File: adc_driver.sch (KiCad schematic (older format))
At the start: 30 parts, among them U17 DG412xUE, U18 AD8421ARZ, U22 TMUX6136PWR, U24 LMP8350MA_NOPB

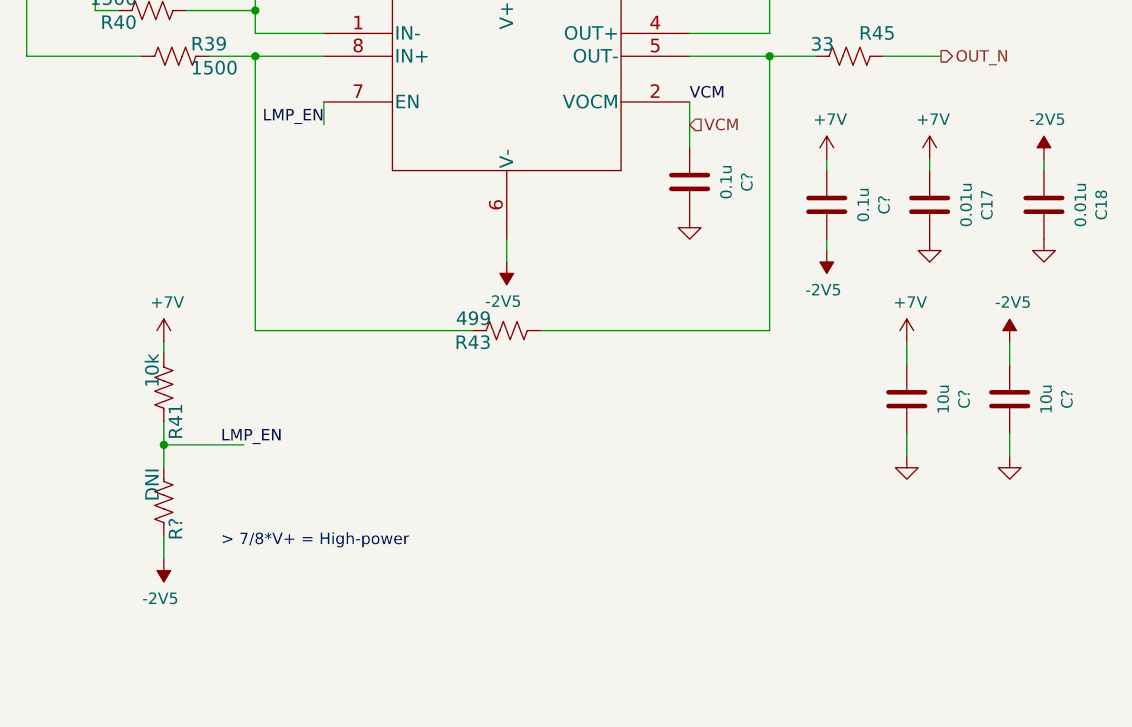
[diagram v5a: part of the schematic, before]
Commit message: clamp files at submission to JLCPCB
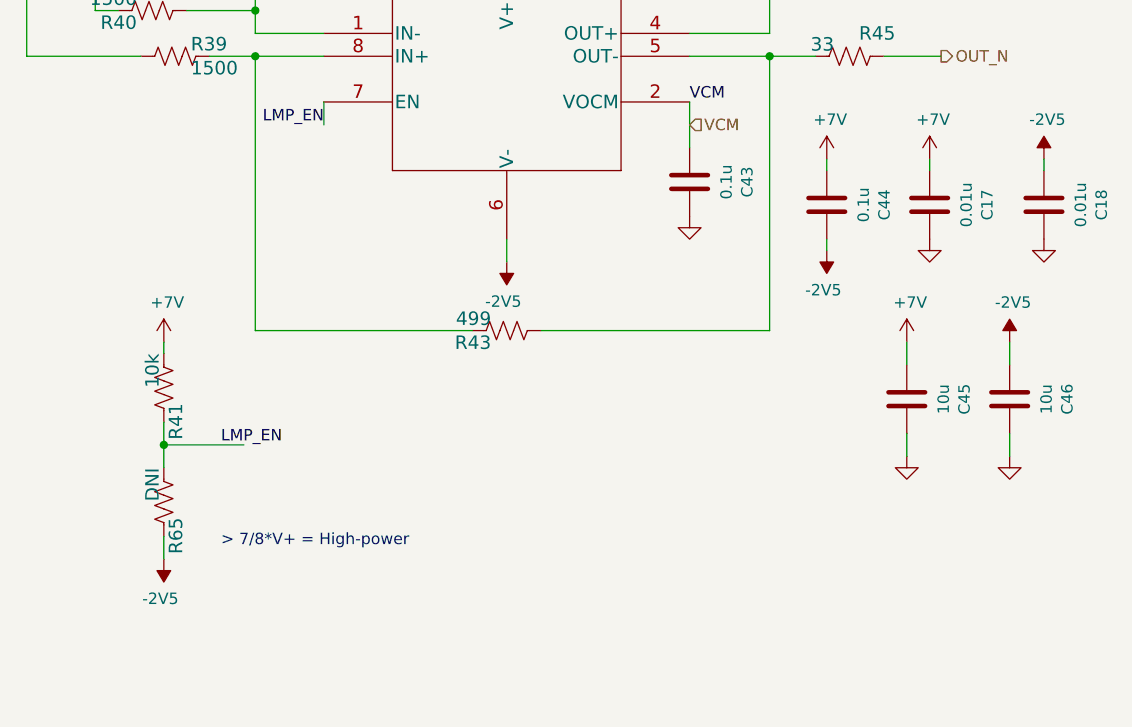
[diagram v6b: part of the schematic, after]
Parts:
- gave numbers to parts that had none: 5
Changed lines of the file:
@@
 U 1 1 60E14CC6
 P 7000 5200
+AR Path="/60E14CC6" Ref="#PWR064"  Part="1"
+AR Path="/6032F251/608FDC40/60E14CC6" Ref="#PWR064"  Part="1"
 F 0 "#PWR064" H 7000 5050 50  0001 C CNN
 F 1 "+7V" H 7015 5373 50  0000 C CNN
@@
 U 1 1 60E2C911
 P 10350 4400
+AR Path="/60E2C911" Ref="#PWR065"  Part="1"
+AR Path="/6032F251/608FDC40/60E2C911" Ref="#PWR065"  Part="1"
 F 0 "#PWR065" H 10350 4250 50  0001 C CNN
 F 1 "+7V" H 10365 4573 50  0000 C CNN
@@
 U 1 1 60B3CD1A
 P 8500 3400
+AR Path="/60B3CD1A" Ref="#PWR0169"  Part="1"
+AR Path="/6032F251/608FDC40/60B3CD1A" Ref="#PWR0169"  Part="1"
 F 0 "#PWR0169" H 8500 3250 50  0001 C CNN
 F 1 "+7V" H 8515 3573 50  0000 C CNN
@@
 P 7000 5900
 AR Path="/6032F251/60EC6475" Ref="R?"  Part="1"
-AR Path="/6032F251/608FDC40/60EC6475" Ref="R?"  Part="1"
-F 0 "R?" V 6947 5968 59  0000 L CNN
+AR Path="/6032F251/608FDC40/60EC6475" Ref="R65"  Part="1"
+F 0 "R65" V 6947 5968 59  0000 L CNN
 F 1 "DNI" V 7050 5750 59  0000 L CNN
 F 2 "Resistor_SMD:R_0603_1608Metric" H 7000 5900 50  0001 C CNN
@@
 $EndComp
 $Comp
-L power:-2V5 #PWR?
+L power:-2V5 #PWR0197
 U 1 1 60ECABF0
 P 7000 6150
-F 0 "#PWR?" H 7000 6250 50  0001 C CNN
+F 0 "#PWR0197" H 7000 6250 50  0001 C CNN
 F 1 "-2V5" H 7015 6323 50  0000 C CNN
 F 2 "" H 7000 6150 50  0001 C CNN
@@
 P 10250 5700
 AR Path="/6032F251/60EDE85E" Ref="#PWR?"  Part="1"
-AR Path="/6032F251/608FDC40/60EDE85E" Ref="#PWR?"  Part="1"
-F 0 "#PWR?" H 10250 5450 50  0001 C CNN
+AR Path="/6032F251/608FDC40/60EDE85E" Ref="#PWR0198"  Part="1"
+F 0 "#PWR0198" H 10250 5450 50  0001 C CNN
 F 1 "GND" V 10255 5572 50  0001 R CNN
 F 2 "" H 10250 5700 50  0001 C CNN
@@
 P 10250 5450
 AR Path="/6032F251/60EDE867" Ref="C?"  Part="1"
-AR Path="/6032F251/608FDC40/60EDE867" Ref="C?"  Part="1"
-F 0 "C?" V 9998 5450 50  0000 C CNN
+AR Path="/6032F251/608FDC40/60EDE867" Ref="C45"  Part="1"
+F 0 "C45" V 9998 5450 50  0000 C CNN
 F 1 "10u" V 10089 5450 50  0000 C CNN
 F 2 "Capacitor_SMD:C_1206_3216Metric" H 10288 5300 50  0001 C CNN
@@
 P 10700 5700
 AR Path="/6032F251/60EEAD1B" Ref="#PWR?"  Part="1"
-AR Path="/6032F251/608FDC40/60EEAD1B" Ref="#PWR?"  Part="1"
-F 0 "#PWR?" H 10700 5450 50  0001 C CNN
+AR Path="/6032F251/608FDC40/60EEAD1B" Ref="#PWR0199"  Part="1"
+F 0 "#PWR0199" H 10700 5450 50  0001 C CNN
 F 1 "GND" V 10705 5572 50  0001 R CNN
 F 2 "" H 10700 5700 50  0001 C CNN
@@
 P 10700 5450
 AR Path="/6032F251/60EEAD24" Ref="C?"  Part="1"
-AR Path="/6032F251/608FDC40/60EEAD24" Ref="C?"  Part="1"
-F 0 "C?" V 10448 5450 50  0000 C CNN
+AR Path="/6032F251/608FDC40/60EEAD24" Ref="C46"  Part="1"
+F 0 "C46" V 10448 5450 50  0000 C CNN
 F 1 "10u" V 10539 5450 50  0000 C CNN
 F 2 "Capacitor_SMD:C_1206_3216Metric" H 10738 5300 50  0001 C CNN
@@
 U 1 1 60EEDCC0
 P 10250 5200
-F 0 "#PWR?" H 10250 5050 50  0001 C CNN
+AR Path="/60EEDCC0" Ref="#PWR?"  Part="1"
+AR Path="/6032F251/608FDC40/60EEDCC0" Ref="#PWR0200"  Part="1"
+F 0 "#PWR0200" H 10250 5050 50  0001 C CNN
 F 1 "+7V" H 10265 5373 50  0000 C CNN
 F 2 "" H 10250 5200 50  0001 C CNN
@@
 $EndComp
 $Comp
-L power:-2V5 #PWR?
+L power:-2V5 #PWR0201
 U 1 1 60EEE112
 P 10700 5200
-F 0 "#PWR?" H 10700 5300 50  0001 C CNN
+F 0 "#PWR0201" H 10700 5300 50  0001 C CNN
 F 1 "-2V5" H 10715 5373 50  0000 C CNN
 F 2 "" H 10700 5200 50  0001 C CNN
@@
 P 9300 4500
 AR Path="/6032F251/60EFA642" Ref="C?"  Part="1"
-AR Path="/6032F251/608FDC40/60EFA642" Ref="C?"  Part="1"
-F 0 "C?" V 9048 4500 50  0000 C CNN
+AR Path="/6032F251/608FDC40/60EFA642" Ref="C43"  Part="1"
+F 0 "C43" V 9048 4500 50  0000 C CNN
 F 1 "0.1u" V 9139 4500 50  0000 C CNN
 F 2 "Capacitor_SMD:C_0603_1608Metric" H 9338 4350 50  0001 C CNN
@@
 P 9300 4650
 AR Path="/6032F251/60EFA648" Ref="#PWR?"  Part="1"
-AR Path="/6032F251/608FDC40/60EFA648" Ref="#PWR?"  Part="1"
-F 0 "#PWR?" H 9300 4400 50  0001 C CNN
+AR Path="/6032F251/608FDC40/60EFA648" Ref="#PWR0202"  Part="1"
+F 0 "#PWR0202" H 9300 4400 50  0001 C CNN
 F 1 "GND" V 9305 4522 50  0001 R CNN
 F 2 "" H 9300 4650 50  0001 C CNN
@@
 P 9900 4600
 AR Path="/6032F251/60F1E80F" Ref="C?"  Part="1"
-AR Path="/6032F251/608FDC40/60F1E80F" Ref="C?"  Part="1"
-F 0 "C?" V 9648 4600 50  0000 C CNN
+AR Path="/6032F251/608FDC40/60F1E80F" Ref="C44"  Part="1"
+F 0 "C44" V 9648 4600 50  0000 C CNN
 F 1 "0.1u" V 9739 4600 50  0000 C CNN
 F 2 "Capacitor_SMD:C_0603_1608Metric" H 9938 4450 50  0001 C CNN
@@
 U 1 1 60F1E81B
 P 9900 4400
-F 0 "#PWR?" H 9900 4250 50  0001 C CNN
+AR Path="/60F1E81B" Ref="#PWR?"  Part="1"
+AR Path="/6032F251/608FDC40/60F1E81B" Ref="#PWR0203"  Part="1"
+F 0 "#PWR0203" H 9900 4250 50  0001 C CNN
 F 1 "+7V" H 9915 4573 50  0000 C CNN
 F 2 "" H 9900 4400 50  0001 C CNN
@@
 	9900 4450 9900 4400
 $Comp
-L power:-2V5 #PWR?
+L power:-2V5 #PWR0204
 U 1 1 60F22200
 P 9900 4800
-F 0 "#PWR?" H 9900 4900 50  0001 C CNN
+F 0 "#PWR0204" H 9900 4900 50  0001 C CNN
 F 1 "-2V5" H 9915 4973 50  0000 C CNN
 F 2 "" H 9900 4800 50  0001 C CNN

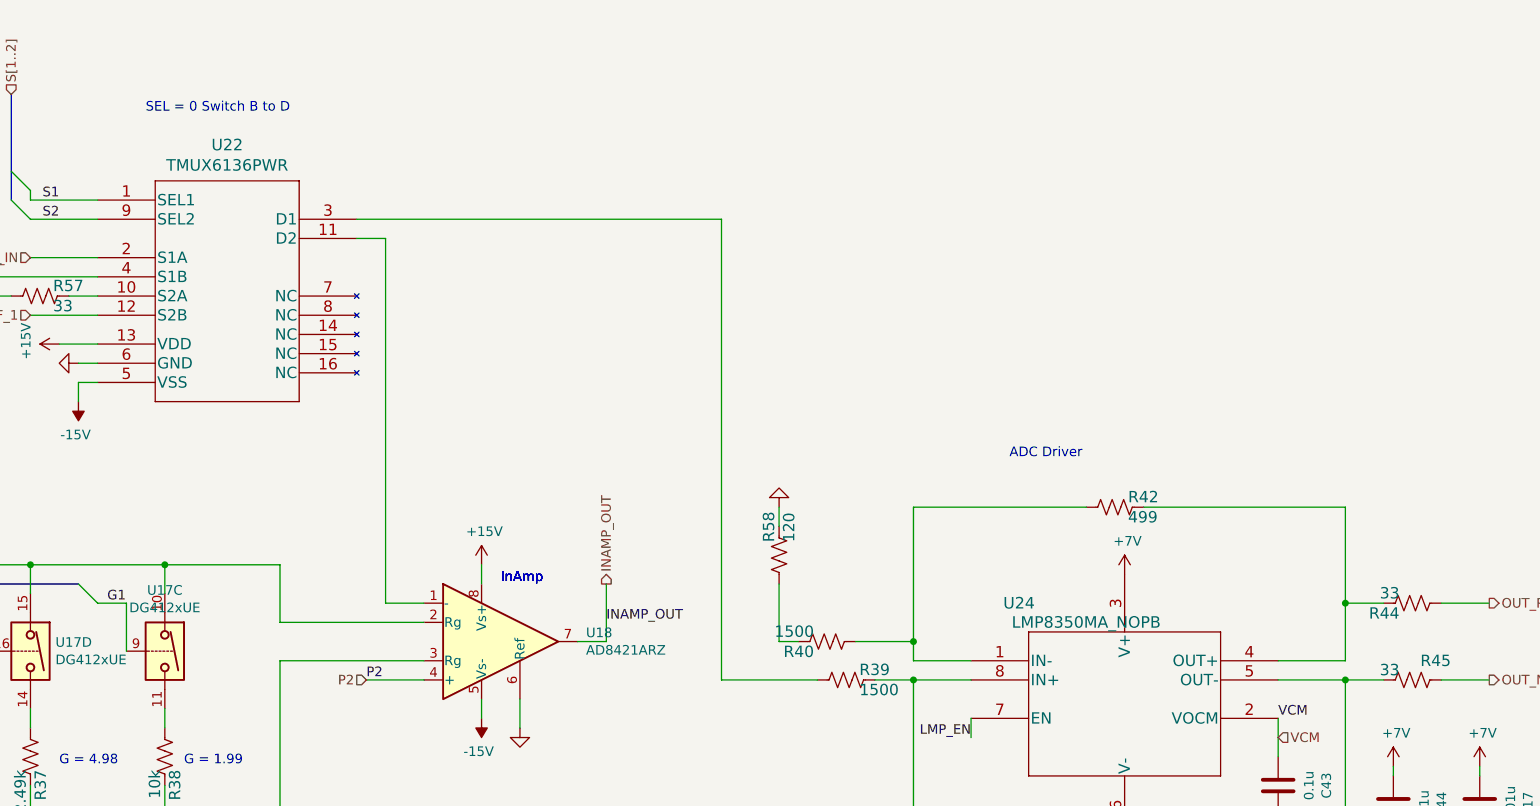
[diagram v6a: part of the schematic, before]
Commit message: updates to schematic for alternate part #s
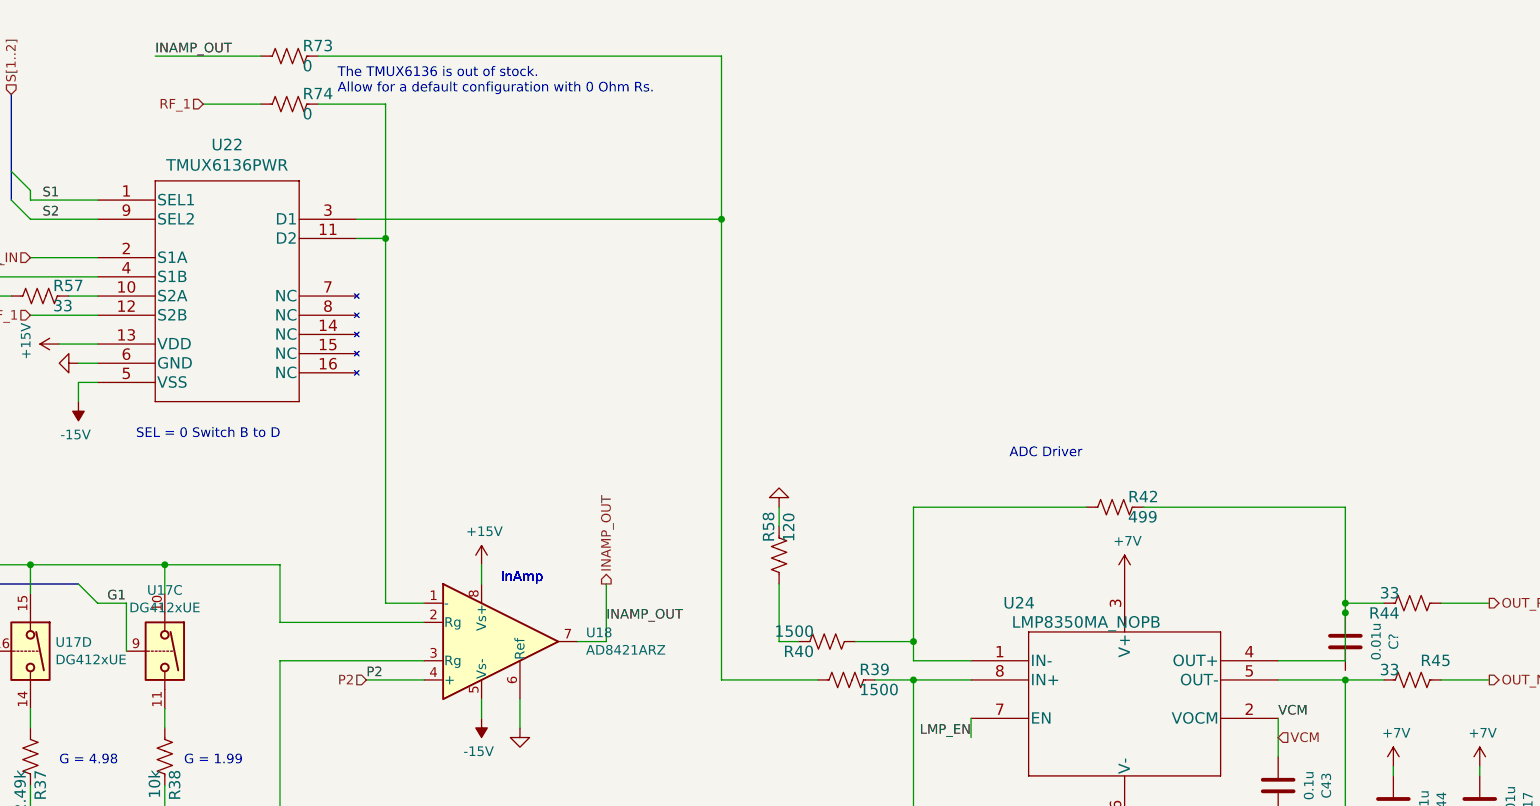
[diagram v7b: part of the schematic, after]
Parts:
- added C?: 0.01u, Capacitor_SMD:C_0603_1608Metric, symbol Device:C
- added R73, R74: 0, Resistor_SMD:R_0603_1608Metric, symbol Device:R_US
- R55, R65: Manf# (none) -> RC0603FR-0710KL
- U17: Alternate Manf# (none) -> TMUX6111PWR; Alternate2 Manf# (none) -> TMUX6112PWR
- U18: footprint Package_SO:TSSOP-8_3x3mm_P0.65mm -> Package_SO:SOIC-8_3.9x4.9mm_P1.27mm; Alternate Manf# (none) -> INA849DR; Alternate2 Manf# (none) -> AD8429ARZ; Manf# AD8421ARMZ -> AD8421ARZ
- U24: Alternate Manf# (none) -> LMP8350MA/NOPB; Alternate2 Manf# (none) -> AD8138AARZ-R7; Manf# LMP8350MA/NOPB -> LMP8350MAX/NOPB
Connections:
- net INAMP_OUT: now also R73.2
- net RF_1: now also R74.2
- net at R39.2, U22.3 (D1): now also R73.1
- net at R42.1, R44.1, U24.4 (OUT+): now also C?.2
- net at U18.1 (-), U22.11 (D2): now also R74.1
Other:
- note added: "ADC Driver \nUsing alternative part LMP8350\nWas ADA4932 (but supply issues)\nLMP8350 max supply of 12 V \n(clamp board design has: 7V + 4V negative)"
- note added: "The TMUX6136 is out of stock.\nAllow for a default configuration with 0 Ohm Rs."
- note removed: "ADC Driver \nUsing alternative part LMP8350\nWas ADA4932 (but supply issues)"
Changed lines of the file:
@@
 F 3 "https://datasheets.maximintegrated.com/en/ds/DG411-DG413.pdf" H 2650 5300 50  0001 C CNN
 F 4 "DG412CUE+" H 2604 5530 50  0001 C CNN "Manf#"
+F 5 "TMUX6111PWR" V 2650 5300 50  0001 C CNN "Alternate Manf#"
+F 6 "TMUX6112PWR" V 2650 5300 50  0001 C CNN "Alternate2 Manf#"
 	5    2650 5300
 	0    1    1    0
@@
 F 3 "https://datasheets.maximintegrated.com/en/ds/DG411-DG413.pdf" H 1350 3800 50  0001 C CNN
 F 4 "DG412CUE+" V 1350 3800 50  0001 C CNN "Manf#"
+F 5 "TMUX6111PWR" V 1350 3800 50  0001 C CNN "Alternate Manf#"
+F 6 "TMUX6112PWR" V 1350 3800 50  0001 C CNN "Alternate2 Manf#"
 	1    1350 3800
 	0    1    1    0
@@
 F 0 "U18" H 5694 3796 50  0000 L CNN
 F 1 "AD8421ARZ" H 5694 3705 50  0000 L CNN
-F 2 "Package_SO:TSSOP-8_3x3mm_P0.65mm" H 5050 3750 50  0001 C CNN
+F 2 "Package_SO:SOIC-8_3.9x4.9mm_P1.27mm" H 5050 3750 50  0001 C CNN
 F 3 "https://www.analog.com/media/en/technical-documentation/data-sheets/AD8421.pdf" H 5600 3350 50  0001 C CNN
-F 4 "AD8421ARMZ" H 5694 3896 50  0001 C CNN "Manf#"
+F 4 "AD8421ARZ" H 5694 3896 50  0001 C CNN "Manf#"
+F 5 "INA849DR" H 5150 3750 50  0001 C CNN "Alternate Manf#"
+F 6 "AD8429ARZ" H 5150 3750 50  0001 C CNN "Alternate2 Manf#"
 	1    5150 3750
 	1    0    0    -1
@@
 VCM
 Text Notes 7900 2800 0    50   ~ 0
-ADC Driver \nUsing alternative part LMP8350\nWas ADA4932 (but supply issues)
+ADC Driver \nUsing alternative part LMP8350\nWas ADA4932 (but supply issues)\nLMP8350 max supply of 12 V \n(clamp board design has: 7V + 4V negative)
 Text HLabel 4550 3950 0    50   Input ~ 0
 P2
@@
 F 2 "Resistor_SMD:R_0603_1608Metric" H 700 3950 50  0001 C CNN
 F 3 "" H 700 3950 50  0001 C CNN
-F 4 "" H 647 4118 50  0001 C CNN "Manf#"
+F 4 "RC0603FR-0710KL" H 647 4118 50  0001 C CNN "Manf#"
 F 5 "1%" H 700 3950 50  0001 C CNN "Tolerance"
 	1    700  3950
@@
 Wire Wire Line
 	4500 1650 4650 1650
-Wire Wire Line
-	4650 1650 4650 3550
 Wire Wire Line
 	4650 3550 4850 3550
@@
 F 2 "Package_SO:SOIC-8_3.9x4.9mm_P1.27mm" H 8200 3750 60  0001 C CNN
 F 3 "" H 7700 3650 60  0000 C CNN
-F 4 "LMP8350MA/NOPB" H 7700 3650 50  0001 C CNN "Manf#"
+F 4 "LMP8350MAX/NOPB" H 7700 3650 50  0001 C CNN "Manf#"
+F 5 "LMP8350MA/NOPB" H 7700 3650 50  0001 C CNN "Alternate Manf#"
+F 6 "AD8138AARZ-R7" H 7700 3650 50  0001 C CNN "Alternate2 Manf#"
 	1    7700 3650
 	1    0    0    -1
@@
 	9650 3850 9300 3850
 Wire Wire Line
-	9650 3550 9650 3850
+	9650 3550 9650 3600
 Wire Wire Line
 	2800 1450 3150 1450
@@
 Text Notes 4800 6800 0    50   ~ 0
 4.7 uF for the AD8421 inamp
-Text Notes 3400 1000 0    50   ~ 0
+Text Notes 3350 2700 0    50   ~ 0
 SEL = 0 Switch B to D\n SEL = 1 Switch A to D
 Text Label 7700 4250 2    50   ~ 0
@@
 F 2 "Resistor_SMD:R_0603_1608Metric" H 7000 5900 50  0001 C CNN
 F 3 "" H 7000 5900 50  0001 C CNN
-F 4 "" H 6947 6068 50  0001 C CNN "Manf#"
+F 4 "RC0603FR-0710KL" H 6947 6068 50  0001 C CNN "Manf#"
 F 5 "5%" H 7000 5900 50  0001 C CNN "Tolerance"
 	1    7000 5900
@@
 Wire Wire Line
 	9900 4750 9900 4800
+$Comp
+L Device:R_US R?
+U 1 1 624E2110
+P 4150 700
+AR Path="/6032F251/624E2110" Ref="R?"  Part="1"
+AR Path="/6032F251/608FDC40/624E2110" Ref="R73"  Part="1"
+F 0 "R73" V 4097 768 59  0000 L CNN
+F 1 "0" V 4202 768 59  0000 L CNN
+F 2 "Resistor_SMD:R_0603_1608Metric" H 4150 700 50  0001 C CNN
+F 3 "" H 4150 700 50  0001 C CNN
+F 4 "RC0603FR-070RL" H 4097 868 50  0001 C CNN "Manf#"
+F 5 "1%" H 4150 700 50  0001 C CNN "Tolerance"
+	1    4150 700
+	0    1    1    0
+$EndComp
+$Comp
+L Device:R_US R?
+U 1 1 624E35D5
+P 4150 950
+AR Path="/6032F251/624E35D5" Ref="R?"  Part="1"
+AR Path="/6032F251/608FDC40/624E35D5" Ref="R74"  Part="1"
+F 0 "R74" V 4097 1018 59  0000 L CNN
+F 1 "0" V 4202 1018 59  0000 L CNN
+F 2 "Resistor_SMD:R_0603_1608Metric" H 4150 950 50  0001 C CNN
+F 3 "" H 4150 950 50  0001 C CNN
+F 4 "RC0603FR-070RL" H 4097 1118 50  0001 C CNN "Manf#"
+F 5 "1%" H 4150 950 50  0001 C CNN "Tolerance"
+	1    4150 950
+	0    1    1    0
+$EndComp
+Wire Wire Line
+	4300 700  6400 700
+Wire Wire Line
+	6400 700  6400 1550
+Connection ~ 6400 1550
+Text Label 3450 700  0    50   ~ 0
+INAMP_OUT
+Wire Wire Line
+	3450 700  4000 700
+Text HLabel 3700 950  0    50   Input ~ 0
+RF_1
+Wire Wire Line
+	3700 950  4000 950
+Wire Wire Line
+	4300 950  4650 950
+Wire Wire Line
+	4650 950  4650 1650
+Connection ~ 4650 1650
+Wire Wire Line
+	4650 1650 4650 3550
+Text Notes 4400 900  0    50   ~ 0
+The TMUX6136 is out of stock.\nAllow for a default configuration with 0 Ohm Rs.
 Wire Bus Line
 	2700 900  2700 1450
 Wire Bus Line
 	900  3450 3050 3450
+$Comp
+L Device:C C?
+U 1 1 624CB27E
+P 9650 3750
+AR Path="/6032F251/624CB27E" Ref="C?"  Part="1"
+AR Path="/6032F251/608FDC40/624CB27E" Ref="C?"  Part="1"
+F 0 "C?" V 9398 3750 50  0000 C CNN
+F 1 "0.01u" V 9489 3750 50  0000 C CNN
+F 2 "Capacitor_SMD:C_0603_1608Metric" H 9688 3600 50  0001 C CNN
+F 3 "~" H 9650 3750 50  0001 C CNN
+F 4 "CC0603MRX7R8BB103" H 9398 3850 50  0001 C CNN "Manf#"
+F 5 "20%" H 9398 3850 50  0001 C CNN "Tolerance"
+F 6 "25V" H 9398 3850 50  0001 C CNN "voltage"
+	1    9650 3750
+	-1   0    0    1
+$EndComp
+Connection ~ 9650 3600
+Wire Wire Line
+	9650 3600 9650 3850
 $EndSCHEMATC

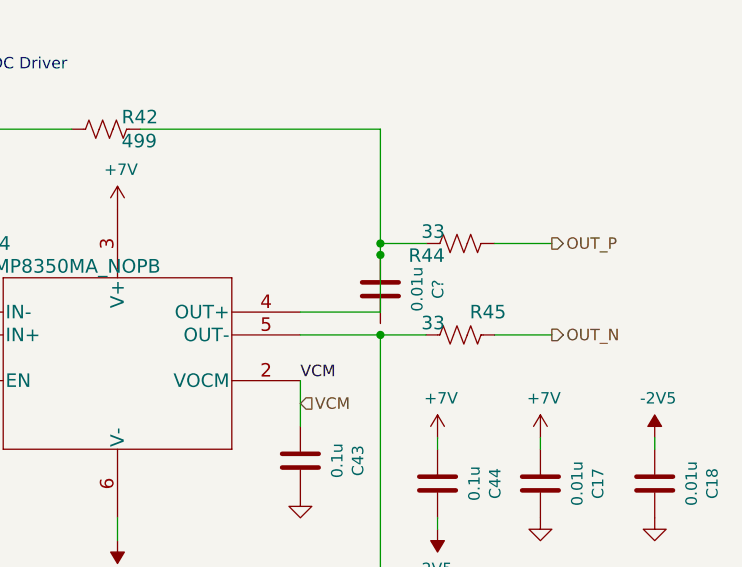
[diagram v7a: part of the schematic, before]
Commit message: nearly completed layout re-route
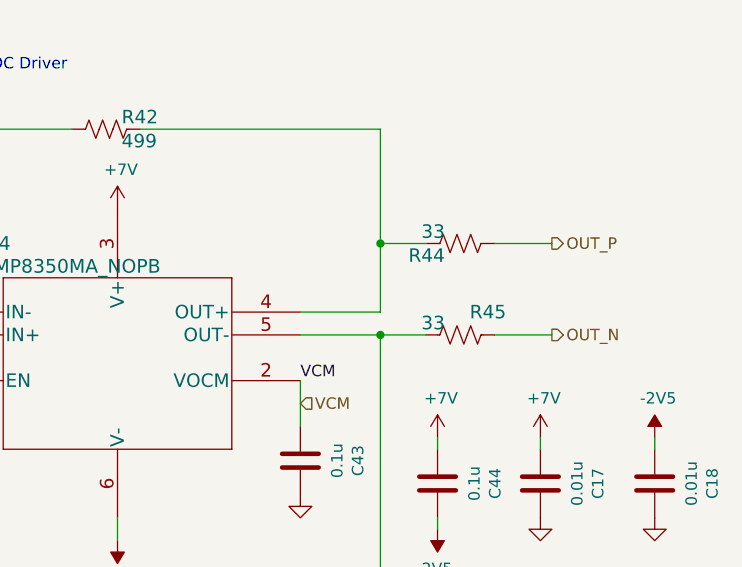
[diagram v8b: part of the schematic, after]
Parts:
- removed C?: 0.01u, Capacitor_SMD:C_0603_1608Metric, symbol Device:C
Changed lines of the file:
@@
 Wire Wire Line
 	9650 3050 9650 3550
-Connection ~ 9650 3550
 Wire Wire Line
 	7400 3050 7400 3750
@@
 Wire Wire Line
 	9650 3850 9300 3850
-Wire Wire Line
-	9650 3550 9650 3600
 Wire Wire Line
 	2800 1450 3150 1450
@@
 Text Notes 4400 900  0    50   ~ 0
 The TMUX6136 is out of stock.\nAllow for a default configuration with 0 Ohm Rs.
+Wire Wire Line
+	9650 3850 9650 3550
+Connection ~ 9650 3550
 Wire Bus Line
 	2700 900  2700 1450
 Wire Bus Line
 	900  3450 3050 3450
-$Comp
-L Device:C C?
-U 1 1 624CB27E
-P 9650 3750
-AR Path="/6032F251/624CB27E" Ref="C?"  Part="1"
-AR Path="/6032F251/608FDC40/624CB27E" Ref="C?"  Part="1"
-F 0 "C?" V 9398 3750 50  0000 C CNN
-F 1 "0.01u" V 9489 3750 50  0000 C CNN
-F 2 "Capacitor_SMD:C_0603_1608Metric" H 9688 3600 50  0001 C CNN
-F 3 "~" H 9650 3750 50  0001 C CNN
-F 4 "CC0603MRX7R8BB103" H 9398 3850 50  0001 C CNN "Manf#"
-F 5 "20%" H 9398 3850 50  0001 C CNN "Tolerance"
-F 6 "25V" H 9398 3850 50  0001 C CNN "voltage"
-	1    9650 3750
-	-1   0    0    1
-$EndComp
-Connection ~ 9650 3600
-Wire Wire Line
-	9650 3600 9650 3850
 $EndSCHEMATC
